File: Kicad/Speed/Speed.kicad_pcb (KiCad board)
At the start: 2 copper layers, 210.8 x 105.4 mm, 48 parts, among them IC1 LK112M60TR, IC10 PI3B3251QE, IC2 AP7365-33WG-7, IC3 LD1117S50C, IC4 DS1813R-10+T&R, IC5 74LVC161PW,112, IC6 74LVC04APW,118, IC7 74LVC138APW-Q100J, IC8 74LVC138APW-Q100J, IC9 SN74CBT3257CPWR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

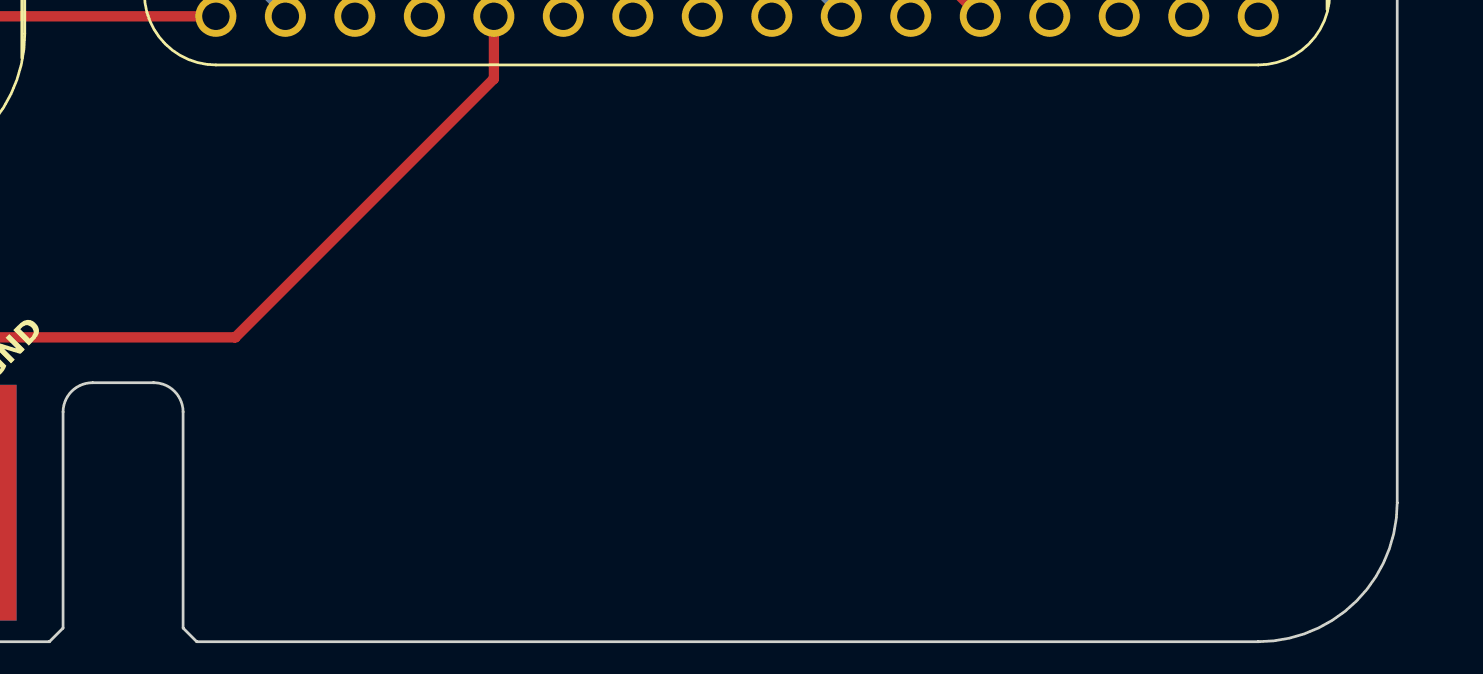
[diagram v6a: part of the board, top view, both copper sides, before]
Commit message: Panelised Speed Board.
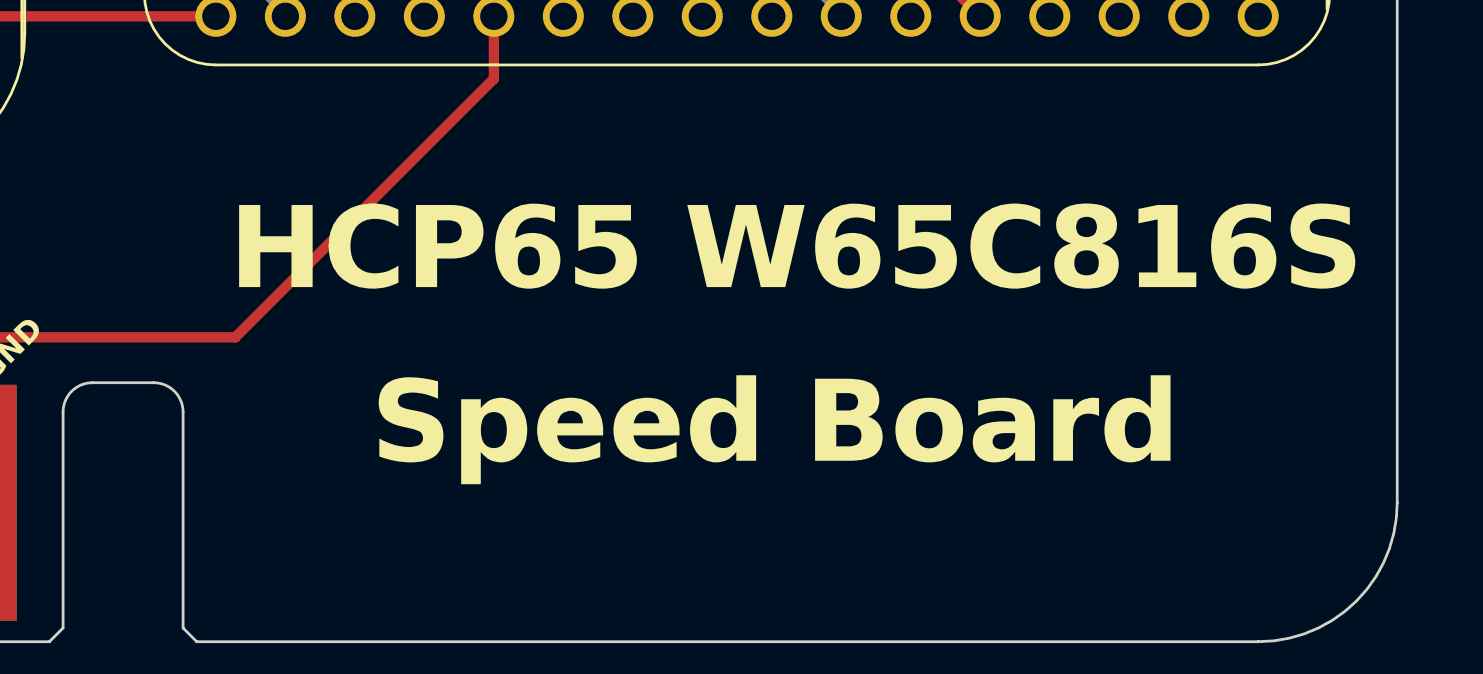
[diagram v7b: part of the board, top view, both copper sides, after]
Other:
- board text added: "HCP65 W65C816S"
- board text added: "Speed Board"
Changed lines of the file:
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@@
 			(drillshape 0)
 			(scaleselection 1)
-			(outputdirectory "Processor Board")
+			(outputdirectory "Speed Board")
 		)
 	)
@@
 		)
 	)
+	(gr_text "HCP65 W65C816S"
+		(at 221.876998 139.319 0)
+		(layer "F.SilkS" knockout)
+		(effects
+			(font
+				(size 3 3)
+				(thickness 0.6)
+				(bold yes)
+			)
+		)
+	)
 	(gr_text "GND"
 		(at 192.539998 144.272 45)
@@
 		)
 	)
+	(gr_text "Speed Board"
+		(at 221.114998 145.669 0)
+		(layer "F.SilkS" knockout)
+		(effects
+			(font
+				(size 3 3)
+				(thickness 0.6)
+				(bold yes)
+			)
+		)
+	)

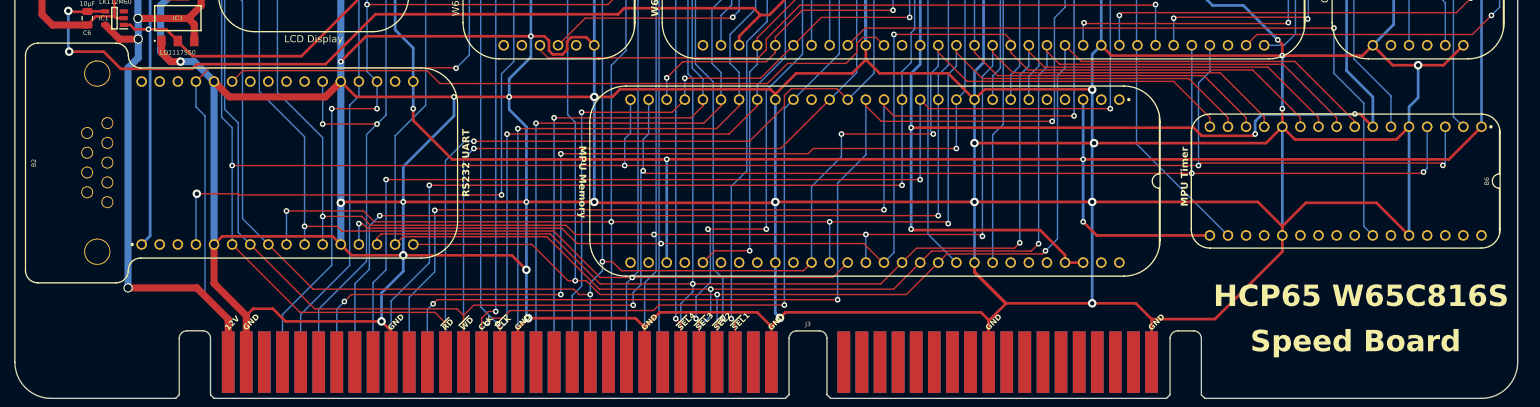
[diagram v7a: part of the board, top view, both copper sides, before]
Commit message: Forgot to clean up traces.  Regenerated video board Gerbers.
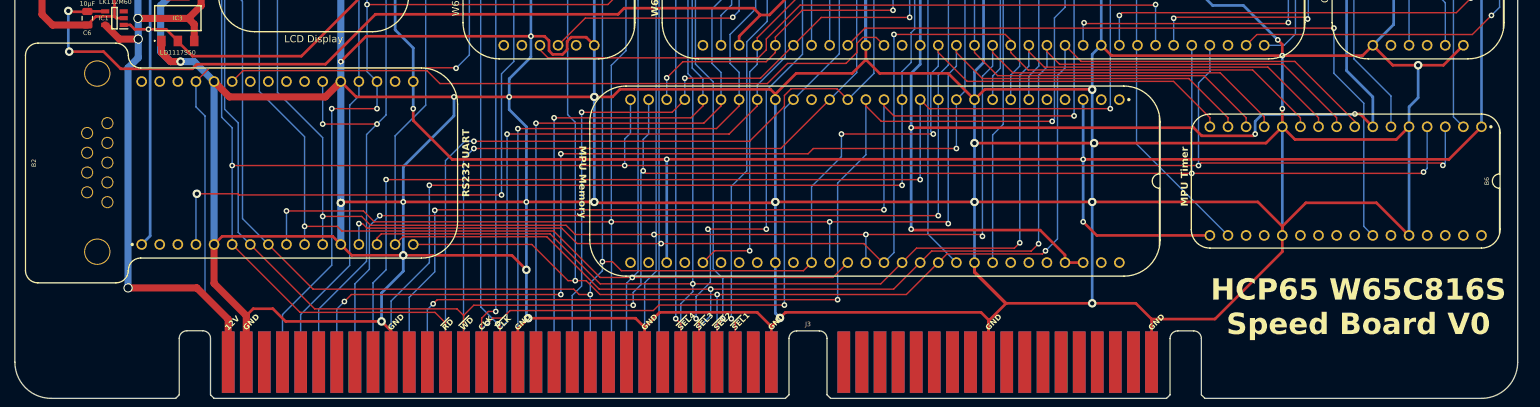
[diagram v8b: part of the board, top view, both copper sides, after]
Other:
- board text added: "HCP65 W65C816S Speed Board V0"
- board text removed: "HCP65 W65C816S"
- board text removed: "Speed Board"
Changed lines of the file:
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@@
 		(fp_arc
 			(start 26.503803 -16.293381)
-			(mid 27.734591 -15.783562)
+			(mid 27.734626 -15.783568)
 			(end 28.244422 -14.552762)
 			(stroke
@@
 		(fp_arc
 			(start 86.040048 -8.4)
-			(mid 86.35762 -9.156489)
+			(mid 86.357626 -9.156454)
 			(end 87.117096 -9.466799)
 			(stroke
@@
 		(fp_arc
 			(start 90.297 -9.466799)
-			(mid 91.056441 -9.156453)
+			(mid 91.056476 -9.156459)
 			(end 91.374048 -8.4)
 			(stroke
@@
 		(fp_arc
 			(start 139.499048 -8.4)
-			(mid 139.81662 -9.156489)
+			(mid 139.816626 -9.156454)
 			(end 140.576096 -9.466799)
 			(stroke
@@
 		(fp_arc
 			(start 14.404267 -2.613733)
-			(mid 16.252451 -1.848184)
+			(mid 16.252448 -1.848183)
 			(end 17.017999 -0.000001)
 			(stroke
@@
 		(fp_arc
 			(start 24.765028 1.905401)
-			(mid 26.252921 -1.686687)
+			(mid 26.252922 -1.686684)
 			(end 29.845 -3.174599)
 			(stroke
@@
 		)
 	)
-	(gr_text "HCP65 W65C816S"
-		(at 221.876998 139.319 0)
+	(gr_text "HCP65 W65C816S\nSpeed Board V0"
+		(at 221.495998 140.843 0)
 		(layer "F.SilkS" knockout)
 		(effects
@@
 		)
 	)
-	(gr_text "Speed Board"
-		(at 221.114998 145.669 0)
-		(layer "F.SilkS" knockout)
-		(effects
-			(font
-				(size 3 3)
-				(thickness 0.6)
-				(bold yes)
-			)
-		)
-	)
